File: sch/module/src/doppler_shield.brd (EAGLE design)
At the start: 46.5 x 40 mm, 46 parts, among them K1 615008143721, U1 OPA2365AID, U2 MAX9031AUK+, U3 TSA7887ARMZ-REEL7, U4 74LVC1G14DCK, U5 74LVC1G17DCK

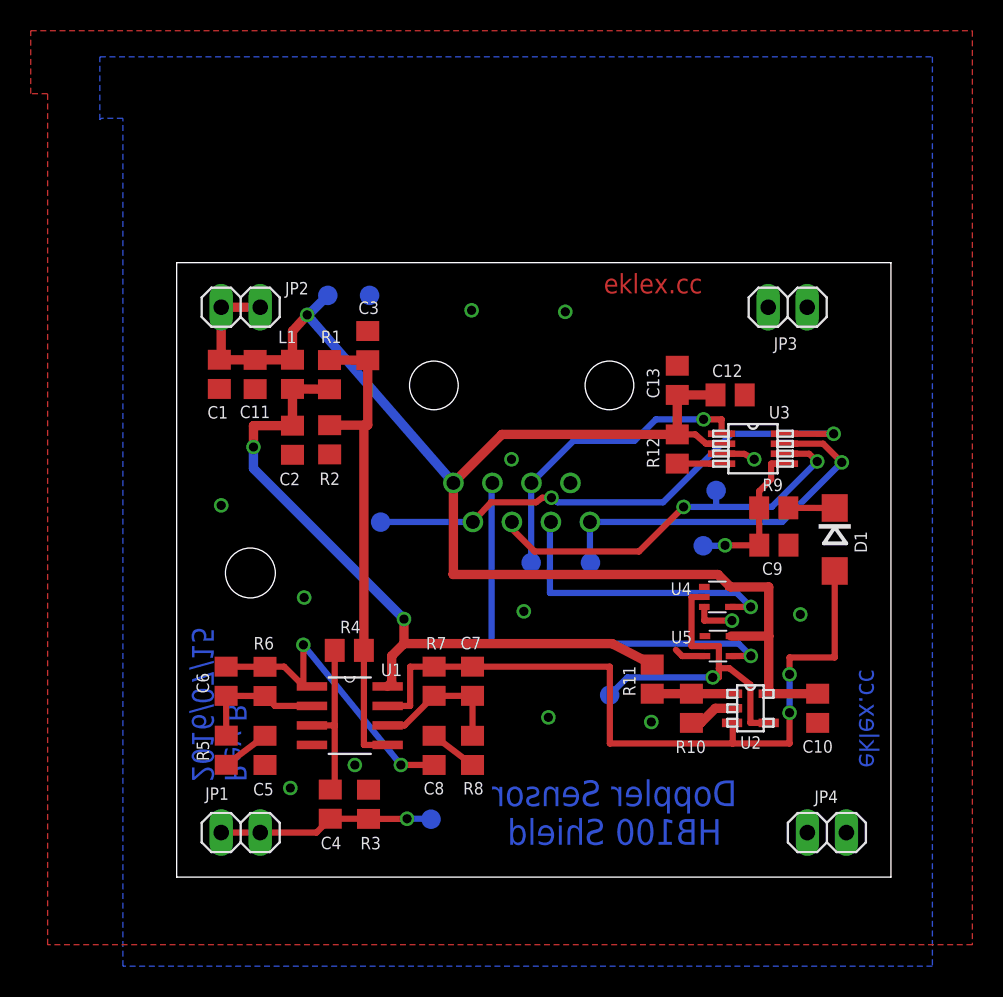
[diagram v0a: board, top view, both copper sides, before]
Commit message: Updated PCB of module card (doppler shield) to revB
  - Fixed JB3 position
  - Added 2 holes aligned on sensor's holes
  - No changes in schematic and BOM
  - Updated revision of SCH, PCB and BOM to revB
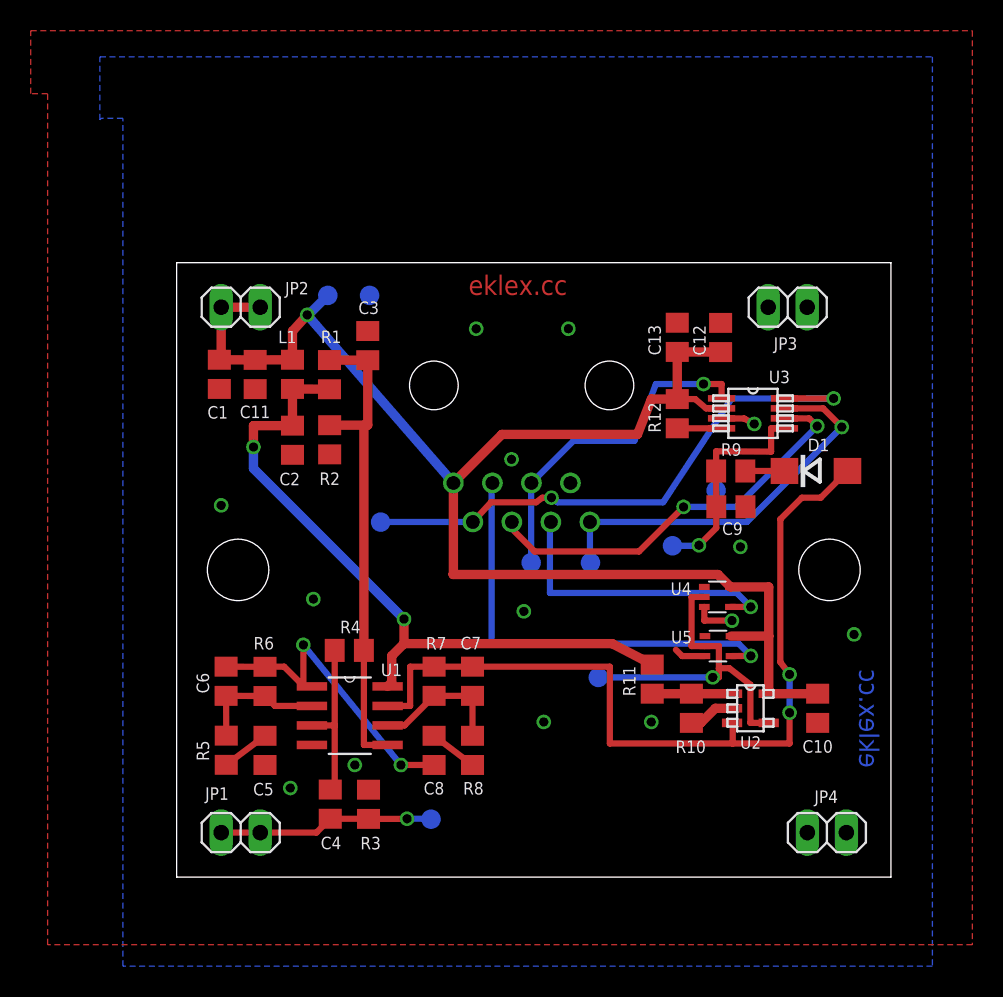
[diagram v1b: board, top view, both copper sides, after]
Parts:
- moved D1 4.62 mm to (41.6, 26.4), turned to 0 degrees
- moved C12 3.79 mm to (35.4, 35.1), turned to 90 degrees
- moved C9 3.75 mm to (36.1, 24.1)
- moved R9 3.69 mm to (36.1, 26.4)
- moved C13 2.80 mm to (32.6, 35.1)
- moved R12 2.30 mm to (32.6, 30.2)
- moved U3 2.30 mm to (37.5, 30.2)
- moved TP8 2.00 mm to (32.3, 21.6)
- moved TP9 1.37 mm to (27.4, 13.0)
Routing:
- net N$19: track 49.3 -> 55.6 mm
- net SENS_OUT: track 10.2 -> 14.3 mm
- net VCC: track 94.0 -> 96.4 mm
- net SPI_CS: track 20.2 -> 22.2 mm
- net SPI_SCK: track 35.3 -> 37.1 mm
- net SPI_MOSI: track 26.8 -> 27.7 mm
- net SPI_MISO: track 24.9 -> 25.9 mm
- net GND: vias 13 -> 14
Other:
- board text added: "Rev B 2017/03/24"
- board text removed: "Rev B 2016/07/15"
